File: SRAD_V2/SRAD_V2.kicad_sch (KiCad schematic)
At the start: 13 parts, among them U11 KX134-1211, U12 MAX-M10S, U13 MS5607-02BA, U14 MMC5983MA, U15 ASM330LHH, U16 MCP9808_DFN, U17 AS5F31G04SND-08LIN, U4 STM32F767ZIT6

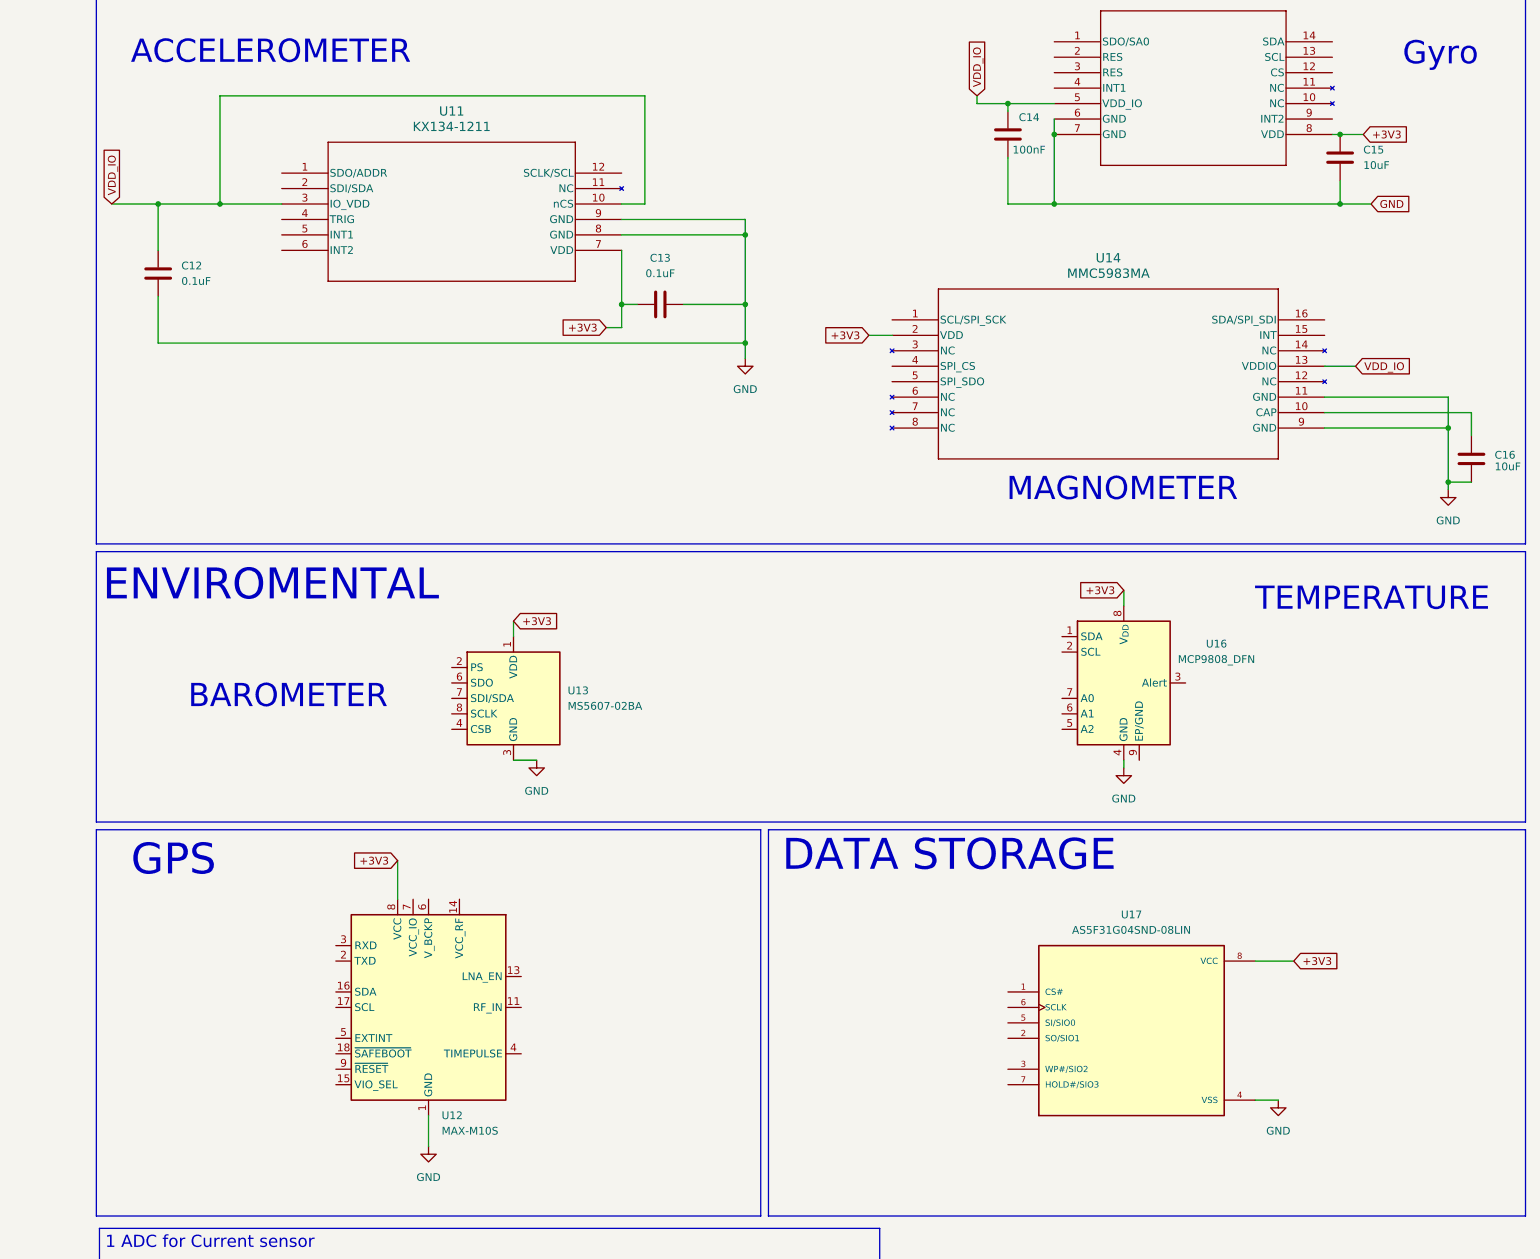
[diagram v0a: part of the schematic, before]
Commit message: added bunch of decoupling capacitors, updated mosfet symbols with KICAD in-built ones etc
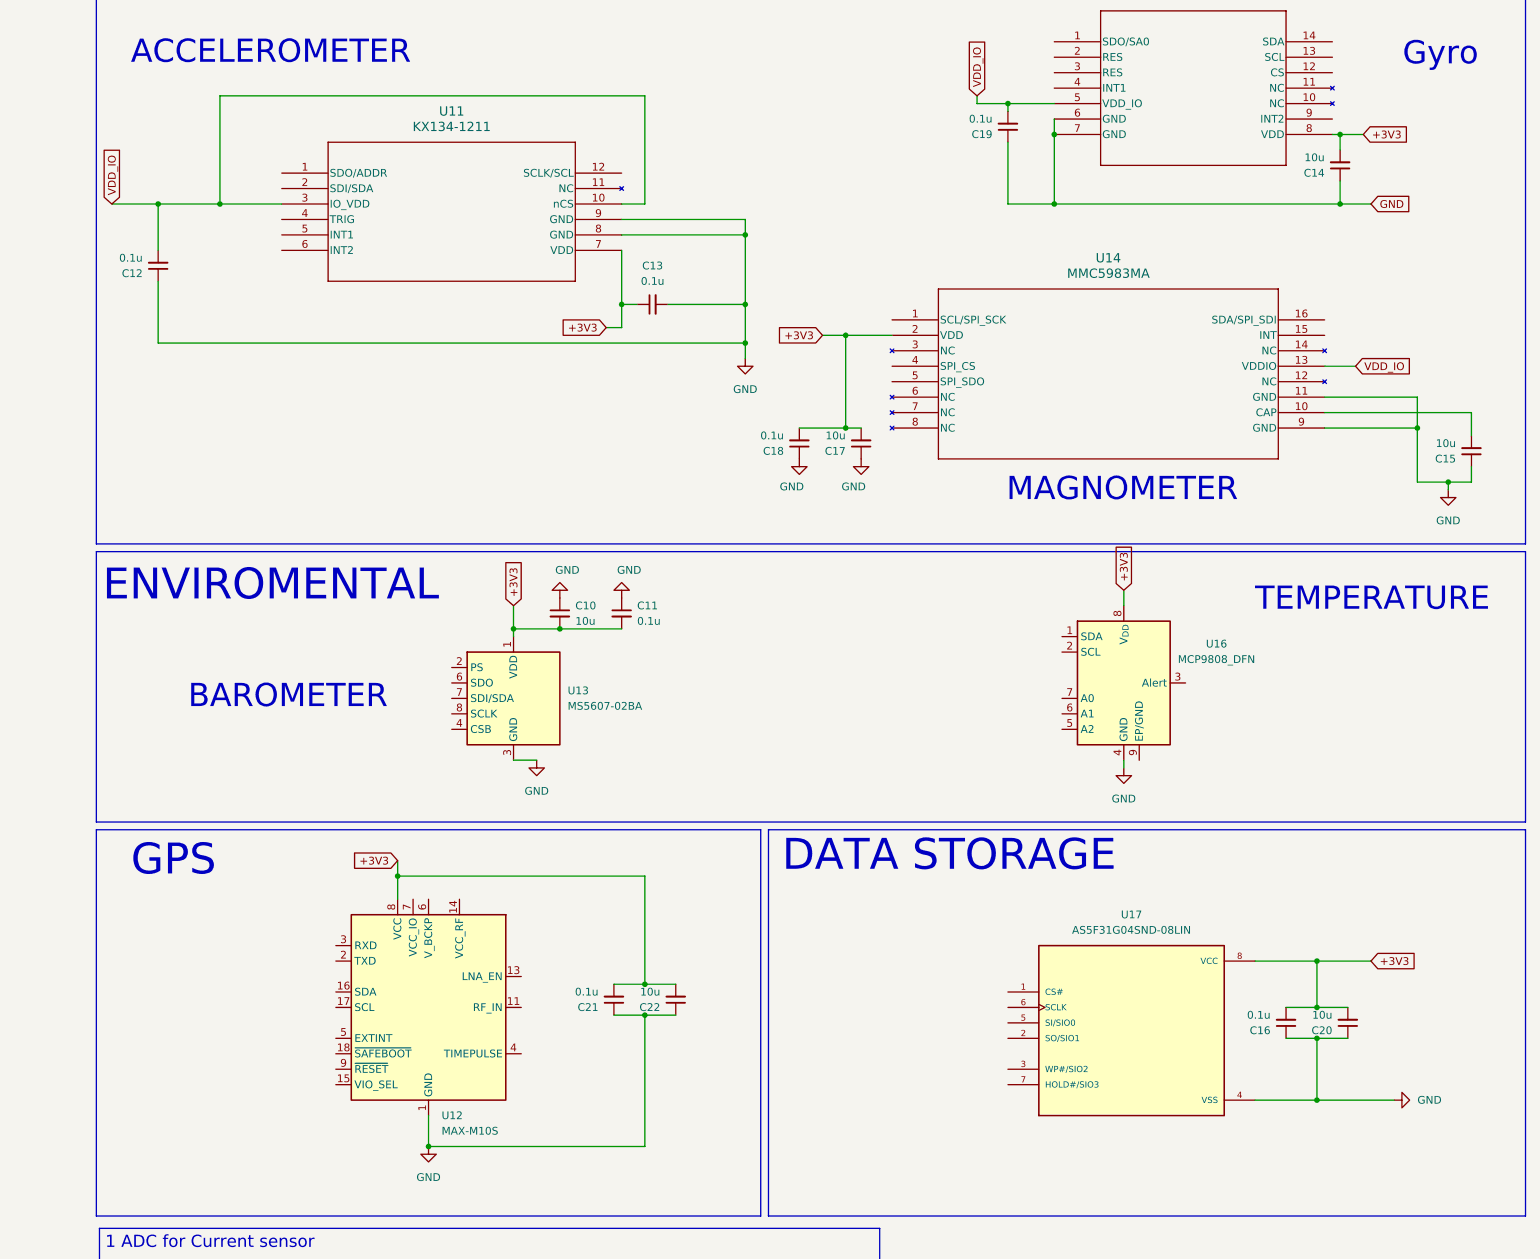
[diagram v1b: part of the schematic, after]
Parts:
- removed C12, C13: 0.1uF, symbol Device:C
- removed C14: 100nF, symbol Device:C
- removed C15, C16: 10uF, symbol Device:C
- added C10, C14, C15, C17, C20, C22: 10u, Capacitor_SMD:C_0603_1608Metric, symbol Device:C_Small
- added C11, C12, C13, C16, C18, C19, C21: 0.1u, Capacitor_SMD:C_0603_1608Metric, symbol Device:C_Small
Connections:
- net +3V3: now also C10.2, C11.2, C13.1, C14.2, C16.2, C17.2, C18.2, C20.2, C21.2, C22.2
- net GND: now also C10.1, C11.1, C12.1, C13.2, C14.1, C15.1, C16.1, C17.1, C18.1, C19.1, C20.1, C21.1, C22.1
- net VDD_IO: now also C12.2, C19.2
- net at U14.10 (CAP): now also C15.2

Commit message: PDS routing
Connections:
- net +3V3: now also C10.1, C11.1; no longer C10.2, C11.2
- net GND: now also C10.2, C11.2; no longer C10.1, C11.1
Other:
- moved on the sheet: C10, C11

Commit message: little tweaks here and there
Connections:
- net +3V3: now also U12.6 (V_BCKP), U12.7 (VCC_IO); no longer U14.2 (VDD)
- net GND: now also U13.2 (PS), U16.9 (EP/GND); no longer U14.11 (GND), U14.9 (GND)
- net VDD_IO: no longer U14.13 (VDDIO)
- net at U14.10 (CAP): no longer C15.2
- net at U14.3 (NC): now also U14.4 (SPI_CS)
- net at U14.6 (NC): now also U14.9 (GND)
- no-connect marks 0 -> 10
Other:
- note added: "interrupt output"
- note added: "spi or i2c"
- moved on the sheet: C12, C13, C14, C15, C17, C18, C19, U11, U15, U16

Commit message: updated MCU cad models
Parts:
- removed U4: STM32F767ZIT6, LQFP144-20x20mm_STM, symbol STM32F767ZIT6:STM32F767ZIT6
- added U1: STM32F767ZITx, Package_QFP:LQFP-144_20x20mm_P0.5mm, symbol MCU_ST_STM32F7:STM32F767ZITx
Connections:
- net +3V3: now also U14.13 (VDDIO), U14.2 (VDD), U1.108 (VDD), U1.131 (VDD), U1.144 (VDD), U1.17 (VDD), U1.30 (VDD), U1.39 (VDD), U1.52 (VDD), U1.62 (VDD), U1.72 (VDD), U1.84 (VDD)
- net GND: now also U14.11 (GND), U14.6 (NC), U14.9 (GND)
- net at U14.10 (CAP): now also C15.2
- new net: U1.107 (VSS), U1.120 (VSS), U1.130 (VSS), U1.16 (VSS), U1.38 (VSS), U1.51 (VSS), U1.61 (VSS), U1.83 (VSS), U1.94 (VSS)
- new net BAROMETER_SCLK: U1.41 (PA5)
- new net BAROMETER_SI: U1.43 (PA7)
- new net BAROMETER_SO: U1.42 (PA6)
- new net GPS_SCL: U1.136 (PB6)
- new net GPS_SDA: U1.137 (PB7)
- new net I_VAL: U1.34 (PA0)
- new net NAND_SPI_CLK: U1.22 (PF10)
- new net NAND_SPI_CS: U1.69 (PB10)
- new net NAND_SPI_IO0: U1.20 (PF8)
- new net NAND_SPI_IO1: U1.21 (PF9)
- new net NAND_SPI_IO2: U1.1 (PE2)
- new net NAND_SPI_IO3: U1.18 (PF6)
- new net TEMP_SCL: U1.11 (PF1)
- new net TEMP_SDA: U1.10 (PF0)
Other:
- note added: "MCU"
- note added: "SENSORS"
- note added: "SUB-CIRCUITS"
- note removed: "ENVIROMENTAL"
- note removed: "IMU & MOTION"
- moved on the sheet: C10, C11, C15, C16, C17, C18, C20, C21, C22, U12, U13, U14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

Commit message: added new IMU to the schematic
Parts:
- added C23, C24: 0.1u, Capacitor_SMD:C_0603_1608Metric, symbol Device:C_Small
- added U4: LSM6DSV80XTR, QFN_LSM6DSV80XTR_STM, symbol LSM6DSV80XTR:LSM6DSV80XTR
- U11, U15, U16: now not fitted
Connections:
- net +3V3: now also C23.1, C24.2, U4.5 (VDDIO), U4.8 (VDD)
- net BAROMETER_SCLK: now also U13.8 (SCLK)
- net BAROMETER_SI: now also U13.7 (SDI/SDA)
- net BAROMETER_SO: now also U13.6 (SDO)
- net GND: now also C23.2, C24.1, U4.2 (SDx), U4.3 (SCx), U4.6 (GND), U4.7 (GND)
- net GPS_SCL: now also U12.17 (SCL)
- net GPS_SDA: now also U12.16 (SDA)
- net NAND_SPI_CLK: now also U17.6 (SCLK)
- net NAND_SPI_CS: now also U17.1 (CS#)
- net NAND_SPI_IO0: now also U17.5 (SI/SIO0)
- net NAND_SPI_IO1: now also U17.2 (SO/SIO1)
- net NAND_SPI_IO2: now also U17.3 (WP#/SIO2)
- net NAND_SPI_IO3: now also U17.7 (HOLD#/SIO3)
- net MAG_SPI_SCK: now reaches U1.111 (PC10)
- net MAG_SPI_SCK: now also U14.1 (SCL/SPI_SCK)
- net IMU_SPI_SDO: now reaches U1.112 (PC11)
- net IMU_SPI_SDO: now also U1.28 (PC2), U4.1 (SDO/TA0)
- net IMU_SPI_SDI: now reaches U1.27 (PC1)
- net IMU_SPI_SDI: now also U4.14 (SDA)
- net MAG_SPI_SDI: now reaches U1.48 (PB2)
- net MAG_SPI_SDI: now also U14.16 (SDA/SPI_SDI)
- net IMU_SPI_SCLK: now reaches U1.74 (PB13)
- net IMU_SPI_SCLK: now also U4.13 (SCL)
- net MAG_SPI_SDO: now reaches U14.5 (SPI_SDO)
- new net IMU_SPI_CS: U4.12 (CS)
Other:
- note added: "IMU"
- note added: "MODE1: Standard 4-wire SPI"
- note added: "Prog. interrupt"
- moved on the sheet: C12, C13, C14, C17, C18, C19

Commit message: Done with Pin Assignments
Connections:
- net IMU_SPI_CS: now also U1.100 (PA8)
- net MAG_SPI_CS: now reaches U1.101 (PA9)
- net MAG_SPI_CS: now also U14.3 (NC), U14.4 (SPI_CS)
- net EM_CH4: now reaches U1.102 (PA10)
- net EM_CH3: now reaches U1.103 (PA11)
- net EM_CH2: now reaches U1.104 (PA12)
- net EM_CH1: now reaches U1.105 (PA13)
- net BAR_SPI_CS: now reaches U1.98 (PC8)
- net BAR_SPI_CS: now also U13.4 (CSB), U13.5 (CSB)
- net TEMP_SCL: no longer names the net of U1.11 (PF1)
- net TEMP_SDA: no longer names the net of U1.10 (PF0)
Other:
- note added: "I2C"

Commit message: added magnometer e-cad model
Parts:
- U14: footprint footprints:MMC5983MA_MEM -> MMC5983MA:MMC5983MA_MEM
- U4: footprint QFN_LSM6DSV80XTR_STM -> MMC5983MA:MMC5983MA_MEM
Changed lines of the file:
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@@
 			)
 		)
-		(property "Footprint" "QFN_LSM6DSV80XTR_STM"
+		(property "Footprint" "MMC5983MA:MMC5983MA_MEM"
 			(at 193.294 138.938 0)
 			(hide yes)
@@
 			)
 		)
-		(property "Footprint" "footprints:MMC5983MA_MEM"
+		(property "Footprint" "MMC5983MA:MMC5983MA_MEM"
 			(at 194.564 91.186 0)
 			(hide yes)

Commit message: sensor routing
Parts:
- added BZ1: Buzzer, buzzer:XDCR_AI-3035-TWT-3V-R, symbol Device:Buzzer
- added C25, C26, C27, C28, C29, C30, C31, C32, C33, C34, C39: 100n, Capacitor_SMD:C_0402_1005Metric_Pad0.74x0.62mm_HandSolder, symbol Device:C_Small
- added C35: 10u, Capacitor_SMD:C_0603_1608Metric, symbol Device:C_Small
- added C36, C38: 1u, Capacitor_SMD:C_0603_1608Metric, symbol Device:C_Small
- added C37: 10n, Capacitor_SMD:C_0402_1005Metric_Pad0.74x0.62mm_HandSolder, symbol Device:C_Small
- added FB1: 120R, symbol Device:FerriteBead
- added R8: 10k, symbol Device:R
- added SW1: SW_Push_Dual, Button_Switch_SMD:SW_DIP_SPSTx02_Slide_6.7x6.64mm_W6.73mm_P2.54mm_LowProfile_JPin, symbol Switch:SW_Push_Dual
- added SW2: SW_Nidec_CAS-120A1, Button_Switch_SMD:Nidec_Copal_CAS-120A, symbol Switch:SW_Nidec_CAS-120A1
- C11, C16, C21, C23, C24: value 0.1u -> 100n
- C12, C13, C19: value 0.1u -> 100n; now not fitted; now left out of the parts list
- C14: now not fitted; now left out of the parts list
- C15, C17: footprint Capacitor_SMD:C_0603_1608Metric -> Capacitor_SMD:C_0402_1005Metric_Pad0.74x0.62mm_HandSolder
- C18: value 0.1u -> 100n; footprint Capacitor_SMD:C_0603_1608Metric -> Capacitor_SMD:C_0402_1005Metric_Pad0.74x0.62mm_HandSolder
- U1: value STM32F767ZITx -> STM32F767ZIT6
- U11, U15, U16: now left out of the parts list
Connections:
- net +3V3: no longer U1.108 (VDD), U1.131 (VDD), U1.144 (VDD), U1.17 (VDD), U1.30 (VDD), U1.39 (VDD), U1.52 (VDD), U1.62 (VDD), U1.72 (VDD), U1.84 (VDD)
- net GND: now also U1.107 (VSS), U1.120 (VSS), U1.130 (VSS), U1.16 (VSS), U1.31 (VSSA), U1.38 (VSS), U1.51 (VSS), U1.61 (VSS), U1.83 (VSS), U1.94 (VSS), C25.2, C26.2, C27.2, C28.2, C29.2, C30.2, C31.2, C32.2, C33.2, C34.2, C35.2, C36.2, C37.2, C38.2, C39.1, SW1.1, SW1.3, SW2.3 (A)
- net at U1.138 (BOOT0): now also SW2.2 (B)
- net at U1.143 (PDR_ON): now also R8.1
- net at U1.25 (NRST): now also C39.2, SW1.2, SW1.4
- net +3.3VA: now reaches U1.33 (VDDA)
- net +3.3VA: now also C37.1, C38.1, FB1.1
- net +3.3V: now reaches U1.6 (VBAT)
- net +3.3V: now also U1.108 (VDD), U1.131 (VDD), U1.144 (VDD), U1.17 (VDD), U1.30 (VDD), U1.39 (VDD), U1.52 (VDD), U1.62 (VDD), U1.72 (VDD), U1.84 (VDD), C25.1, C26.1, C27.1, C28.1, C29.1, C30.1, C31.1, C32.1, C33.1, C34.1, C35.1, C36.1, FB1.2, R8.2, SW2.1 (C)
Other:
- note added: "1*10uF + 100nF(for each VDD pin)"
- note added: "Separate High Freq Filtering for ADCs"
- moved on the sheet: U1
